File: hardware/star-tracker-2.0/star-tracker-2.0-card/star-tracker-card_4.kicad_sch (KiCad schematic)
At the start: 22 parts, among them U1 RCLAMP0504FB, U7 OSD3358-512M-BSM, Y1 ECS-240-12-30BQ-AEN-TR, Y2 ABS07-32.768KHZ-T

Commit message: Routine Push
Updated schematic and layout. about 60% done with routing.
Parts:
- removed TP133, TP138, TP139, TP141: TEST-POINT3X4, oresat-misc:TestPoint_Pad_D1.0mm, symbol oresat-misc:Test-Point-1mm-round
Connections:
- no-connect marks 12 -> 16

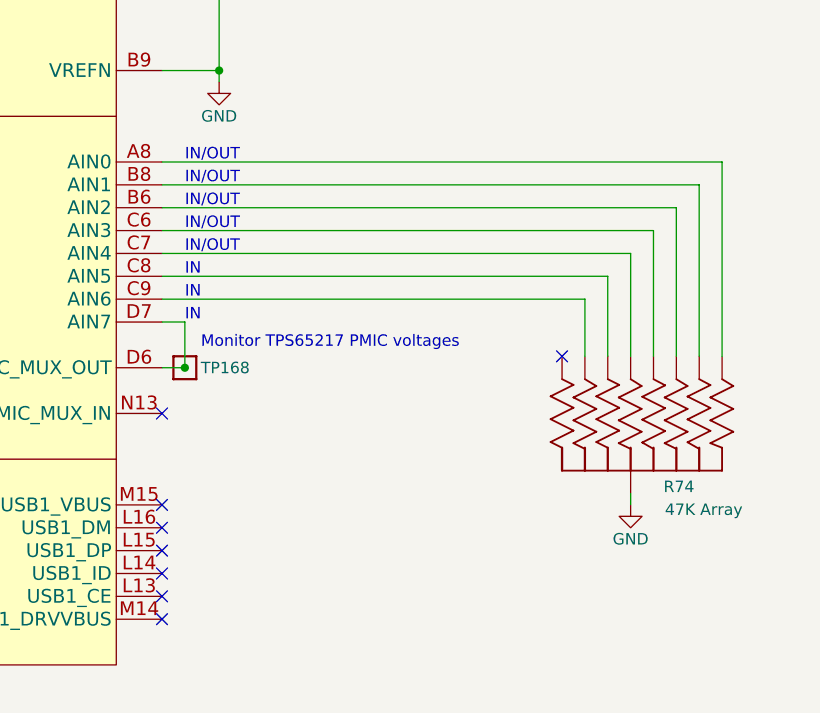
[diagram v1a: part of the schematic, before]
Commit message: Star Tracker 2.0
Layout and routing 100% completed. Only needs minor adjustments for silkscreen and camera mounting holes.
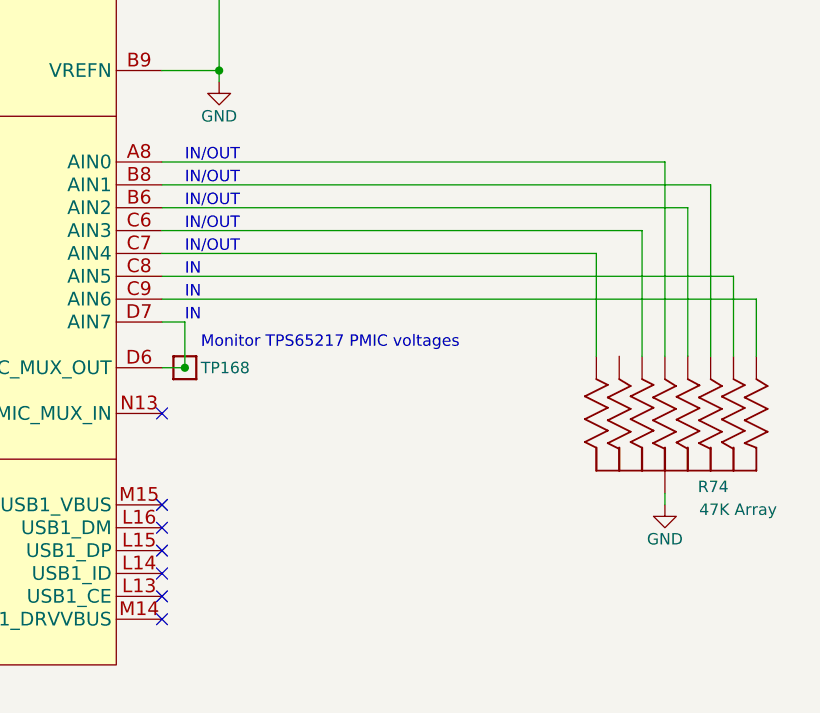
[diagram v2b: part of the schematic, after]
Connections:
- net at R74.1 (11): now also U7.C9 (AIN6); no longer U7.A8 (AIN0)
- net at R74.2 (22): now also U7.B8 (AIN1); no longer U7.B6 (AIN2)
- net at R74.3 (33): now also U7.A8 (AIN0); no longer U7.C7 (AIN4)
- net at R74.4 (44): no longer U7.C9 (AIN6)
- net at R74.6 (66): now also U7.C7 (AIN4)
- net at R74.7 (77): now also U7.C6 (AIN3); no longer U7.C8 (AIN5)
- net at R74.8 (88): now also U7.B6 (AIN2); no longer U7.C6 (AIN3)
- net at R74.9 (99): now also U7.C8 (AIN5); no longer U7.B8 (AIN1)
- no-connect marks 16 -> 15
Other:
- moved on the sheet: R74
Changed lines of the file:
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@@
 	)
 	(no_connect
-		(at 293.37 123.19)
-	)
-	(no_connect
 		(at 248.92 129.54)
 	)
@@
 	(wire
 		(pts
-			(xy 176.53 127) (xy 187.96 127)
+			(xy 312.42 114.3) (xy 248.92 114.3)
 		)
 		(stroke
@@
 	(wire
 		(pts
-			(xy 172.72 113.03) (xy 172.72 114.3)
+			(xy 176.53 127) (xy 187.96 127)
 		)
 		(stroke
@@
 	(wire
 		(pts
-			(xy 306.07 106.68) (xy 306.07 123.19)
+			(xy 172.72 113.03) (xy 172.72 114.3)
 		)
 		(stroke
@@
 	(wire
 		(pts
-			(xy 248.92 101.6) (xy 311.15 101.6)
+			(xy 248.92 101.6) (xy 304.8 101.6)
 		)
 		(stroke
@@
 	(wire
 		(pts
-			(xy 303.53 109.22) (xy 303.53 123.19)
-		)
-		(stroke
-			(width 0)
-			(type default)
-		)
-	)
-	(wire
-		(pts
 			(xy 152.4 142.24) (xy 187.96 142.24)
 		)
@@
 	(wire
 		(pts
-			(xy 147.32 53.34) (xy 152.4 53.34)
+			(xy 297.18 111.76) (xy 297.18 123.19)
 		)
 		(stroke
-			(width 0.1524)
-			(type solid)
+			(width 0)
+			(type default)
 		)
 	)
 	(wire
 		(pts
-			(xy 308.61 104.14) (xy 308.61 123.19)
+			(xy 147.32 53.34) (xy 152.4 53.34)
 		)
 		(stroke
-			(width 0)
-			(type default)
+			(width 0.1524)
+			(type solid)
 		)
 	)
@@
 	(wire
 		(pts
-			(xy 248.92 106.68) (xy 306.07 106.68)
+			(xy 248.92 106.68) (xy 307.34 106.68)
 		)
 		(stroke
@@
 	(wire
 		(pts
+			(xy 307.34 106.68) (xy 307.34 123.19)
+		)
+		(stroke
+			(width 0)
+			(type default)
+		)
+	)
+	(wire
+		(pts
+			(xy 312.42 114.3) (xy 312.42 123.19)
+		)
+		(stroke
+			(width 0)
+			(type default)
+		)
+	)
+	(wire
+		(pts
 			(xy 167.64 198.12) (xy 167.64 195.58)
 		)
@@
 	(wire
 		(pts
-			(xy 300.99 138.43) (xy 300.99 139.7)
+			(xy 302.26 109.22) (xy 302.26 123.19)
+		)
+		(stroke
+			(width 0)
+			(type default)
+		)
+	)
+	(wire
+		(pts
+			(xy 304.8 138.43) (xy 304.8 139.7)
 		)
 		(stroke
@@
 	(wire
 		(pts
-			(xy 300.99 111.76) (xy 300.99 123.19)
+			(xy 248.92 81.28) (xy 255.27 81.28)
 		)
 		(stroke
@@
 	(wire
 		(pts
-			(xy 248.92 81.28) (xy 255.27 81.28)
+			(xy 309.88 123.19) (xy 309.88 104.14)
 		)
 		(stroke
@@
 	(wire
 		(pts
-			(xy 295.91 116.84) (xy 248.92 116.84)
+			(xy 248.92 116.84) (xy 314.96 116.84)
 		)
 		(stroke
@@
 	(wire
 		(pts
-			(xy 298.45 114.3) (xy 298.45 123.19)
-		)
-		(stroke
-			(width 0)
-			(type default)
-		)
-	)
-	(wire
-		(pts
 			(xy 248.92 119.38) (xy 251.46 119.38)
 		)
@@
 	(wire
 		(pts
-			(xy 295.91 116.84) (xy 295.91 123.19)
-		)
-		(stroke
-			(width 0)
-			(type default)
-		)
-	)
-	(wire
-		(pts
 			(xy 168.91 114.3) (xy 172.72 114.3)
 		)
@@
 	(wire
 		(pts
-			(xy 248.92 111.76) (xy 300.99 111.76)
+			(xy 248.92 111.76) (xy 297.18 111.76)
 		)
 		(stroke
@@
 	(wire
 		(pts
-			(xy 255.27 60.96) (xy 255.27 50.8)
+			(xy 314.96 123.19) (xy 314.96 116.84)
 		)
 		(stroke
@@
 	(wire
 		(pts
-			(xy 167.64 167.64) (xy 180.34 167.64)
+			(xy 255.27 60.96) (xy 255.27 50.8)
 		)
 		(stroke
-			(width 0.1524)
-			(type solid)
+			(width 0)
+			(type default)
 		)
 	)
 	(wire
 		(pts
-			(xy 134.62 73.66) (xy 134.62 68.58)
+			(xy 167.64 167.64) (xy 180.34 167.64)
 		)
 		(stroke
@@
 	(wire
 		(pts
-			(xy 311.15 101.6) (xy 311.15 123.19)
+			(xy 134.62 73.66) (xy 134.62 68.58)
 		)
 		(stroke
-			(width 0)
-			(type default)
+			(width 0.1524)
+			(type solid)
 		)
 	)
 	(wire
 		(pts
-			(xy 248.92 114.3) (xy 298.45 114.3)
+			(xy 304.8 101.6) (xy 304.8 123.19)
 		)
 		(stroke
@@
 	(wire
 		(pts
-			(xy 248.92 104.14) (xy 308.61 104.14)
-		)
-		(stroke
-			(width 0)
-			(type default)
-		)
-	)
-	(wire
-		(pts
 			(xy 162.56 124.46) (xy 187.96 124.46)
 		)
@@
 	(wire
 		(pts
+			(xy 248.92 104.14) (xy 309.88 104.14)
+		)
+		(stroke
+			(width 0)
+			(type default)
+		)
+	)
+	(wire
+		(pts
 			(xy 162.56 86.36) (xy 162.56 88.9)
 		)
@@
 	(wire
 		(pts
-			(xy 248.92 109.22) (xy 303.53 109.22)
+			(xy 248.92 109.22) (xy 302.26 109.22)
 		)
 		(stroke
@@
 	(symbol
 		(lib_id "star-tracker-card-eagle-import:EXB-A10P391JC_ARRAY_EXBA-M")
-		(at 311.15 135.89 270)
+		(at 314.96 135.89 270)
 		(unit 1)
 		(body_style 1)
@@
 		(dnp no)
 		(property "Reference" "R74"
-			(at 304.6476 138.43 90)
+			(at 308.4576 138.43 90)
 			(show_name no)
 			(do_not_autoplace no)
@@
 		)
 		(property "Value" "47K Array"
-			(at 304.8 140.97 90)
+			(at 308.61 140.97 90)
 			(show_name no)
 			(do_not_autoplace no)
@@
 		)
 		(property "Footprint" "star-tracker-card:ARRAY_EXBA-M"
-			(at 311.15 135.89 0)
+			(at 314.96 135.89 0)
 			(hide yes)
 			(show_name no)
@@
 		)
 		(property "Datasheet" "http://www.vishay.com/docs/31509/csc.pdf"
-			(at 311.15 135.89 0)
+			(at 314.96 135.89 0)
 			(hide yes)
 			(show_name no)
@@
 		)
 		(property "Description" "47k Ohm ±5% 62.5mW Power Per Element Bussed 8 Resistor Network/Array ±200ppm/°C 2512 (6432 Metric), Concave, Long Side Terminals"
-			(at 311.15 135.89 0)
+			(at 314.96 135.89 0)
 			(hide yes)
 			(show_name no)
@@
 		)
 		(property "DPN" "U7473CT-ND"
-			(at 311.15 135.89 0)
+			(at 314.96 135.89 0)
 			(hide yes)
 			(show_name no)
@@
 		)
 		(property "MPN" "EXB-A10P473J"
-			(at 311.15 135.89 0)
+			(at 314.96 135.89 0)
 			(hide yes)
 			(show_name no)
@@
 		)
 		(property "DIS" "DigiKey"
-			(at 311.15 135.89 90)
+			(at 314.96 135.89 90)
 			(hide yes)
 			(show_name no)
@@
 		)
 		(property "MFR" "Panasonic Electronic Components"
-			(at 311.15 135.89 90)
+			(at 314.96 135.89 90)
 			(hide yes)
 			(show_name no)
@@
 	(symbol
 		(lib_id "power:GND")
-		(at 300.99 139.7 0)
+		(at 304.8 139.7 0)
 		(unit 1)
 		(body_style 1)
@@
 		(dnp no)
 		(property "Reference" "#PWR5"
-			(at 300.99 146.05 0)
+			(at 304.8 146.05 0)
 			(hide yes)
 			(show_name no)
@@
 		)
 		(property "Value" "GND"
-			(at 300.99 143.51 0)
+			(at 304.8 143.51 0)
 			(show_name no)
 			(do_not_autoplace no)
@@
 		)
 		(property "Footprint" ""
-			(at 300.99 139.7 0)
+			(at 304.8 139.7 0)
 			(hide yes)
 			(show_name no)
@@
 		)
 		(property "Datasheet" ""
-			(at 300.99 139.7 0)
+			(at 304.8 139.7 0)
 			(hide yes)
 			(show_name no)
@@
 		)
 		(property "Description" "Power symbol creates a global label with name \"GND\" , ground"
-			(at 300.99 139.7 0)
+			(at 304.8 139.7 0)
 			(hide yes)
 			(show_name no)
